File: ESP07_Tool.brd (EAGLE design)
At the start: 34 x 36.3 mm, 38 parts

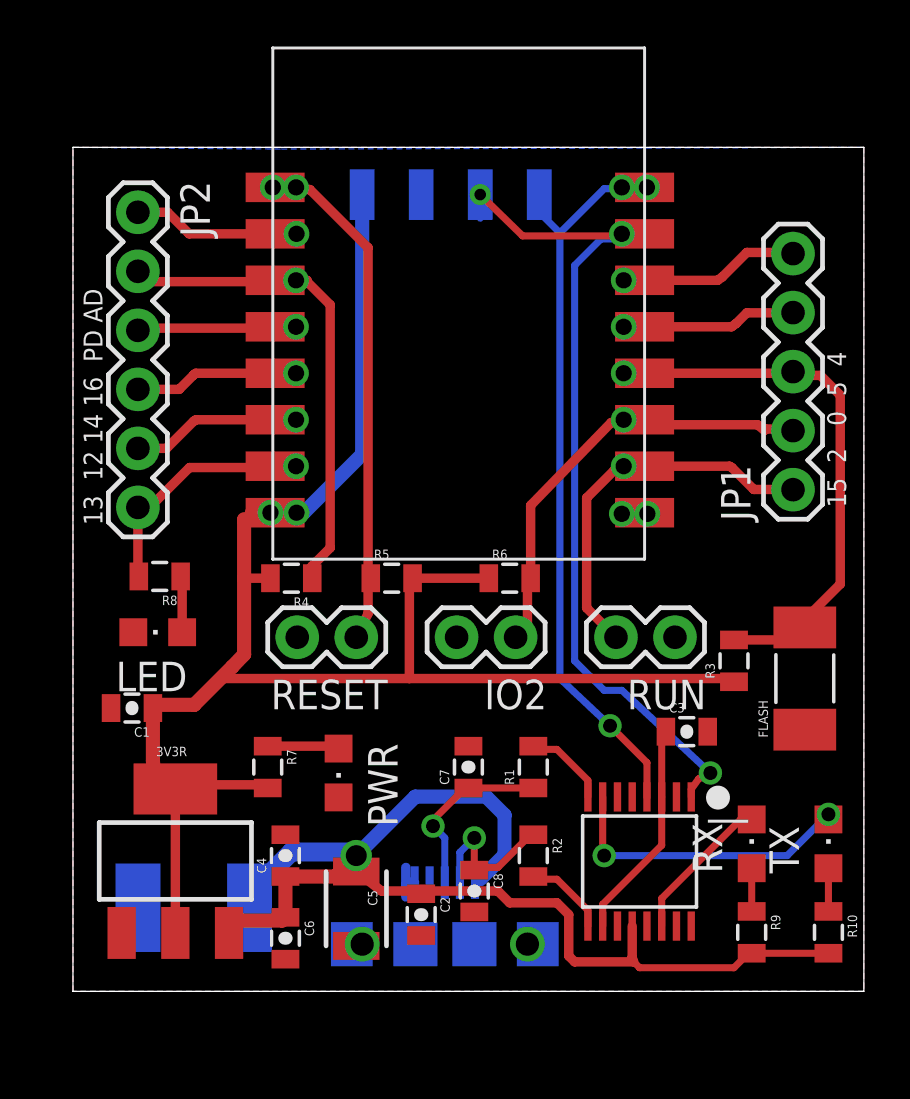
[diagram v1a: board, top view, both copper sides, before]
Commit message: Mods after actual use
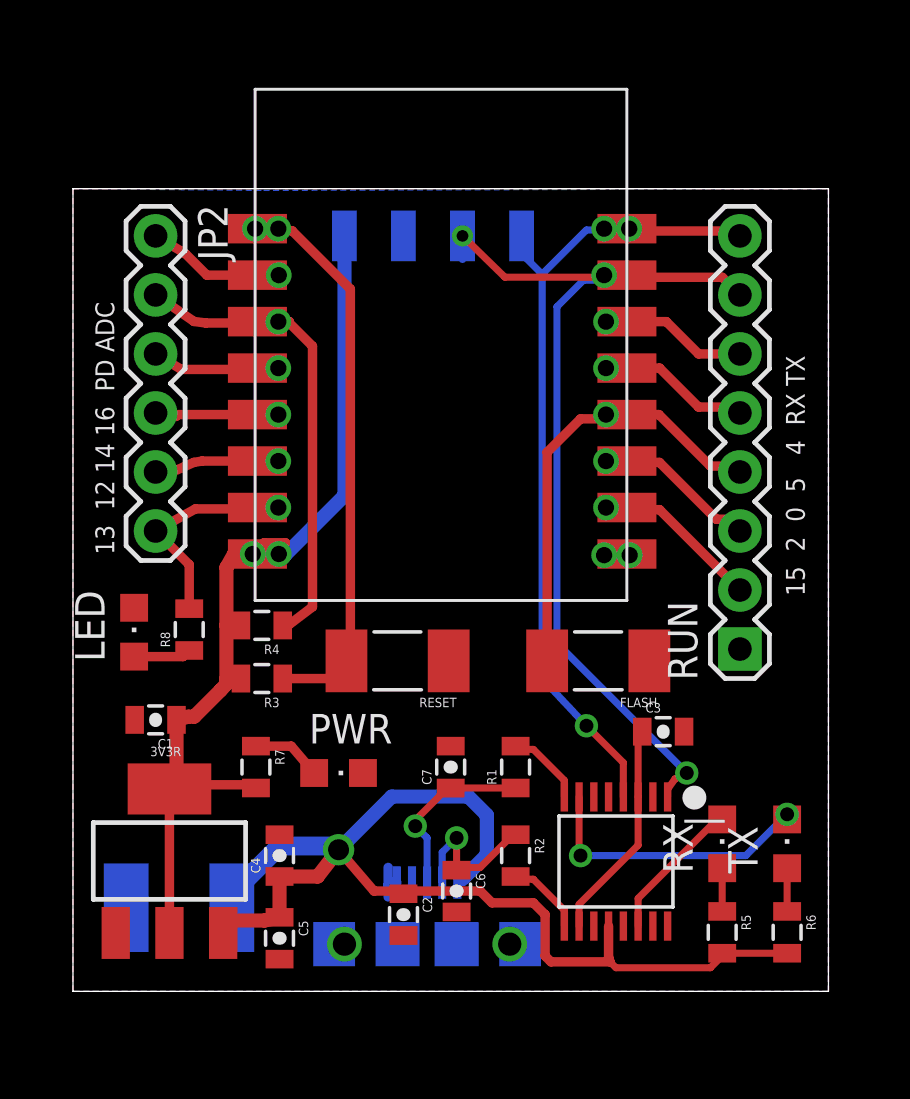
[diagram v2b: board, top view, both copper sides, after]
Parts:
- removed C8: 47pF, SparkFun-Capacitors:0805-CAP
- removed IO2: (no value), SparkFun-Connectors:1X02
- removed JP1: (no value), SparkFun-Connectors:1X05
- removed R10, R9: 330, SparkFun-Resistors:0805
- C1, C2: value 10uF -> 1uF
- C5: value 4.7uF -> 0.1uF; device SparkFun-Capacitors:1210 -> SparkFun-Capacitors:0805-CAP
- C6: value 0.1uF -> 47pF
- R5, R6: value 10K -> 330
- RESET: device SparkFun-Connectors:1X02 -> SparkFun-Resistors:R2010
- RUN: device SparkFun-Connectors:1X02 -> SparkFun-Connectors:1X08
- moved R5 20.8 mm to (27.9, 2.54), turned to 270 degrees
- moved R3 20.3 mm to (8.13, 13.5), turned to 180 degrees
- moved R6 19.4 mm to (30.7, 2.54), turned to 270 degrees
- moved FLASH 8.92 mm to (22.6, 14.2), turned to 180 degrees
- moved C6 7.64 mm to (16.5, 4.32)
- moved C5 3.54 mm to (8.89, 2.29)
- moved RUN 2.84 mm to (28.7, 14.7), turned to 90 degrees
- moved R8 2.62 mm to (5.00, 15.6), turned to 90 degrees
- moved R4 2.40 mm to (8.13, 15.7)
- moved RESET 2.05 mm to (14.0, 14.2)
- moved U$1 1.93 mm to (7.84, 16.8)
- moved U$4 1.93 mm to (16.8, 32.5)
- moved U$5 1.93 mm to (19.3, 32.5)
- moved U$6 1.93 mm to (11.7, 32.5)
- moved U$7 1.93 mm to (14.2, 32.5)
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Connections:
- net 3V3: now also R3.2; no longer R3.1, R5.2, R6.1
- net GND: now also RESET.1; no longer C8.2, IO2.2, RESET.2
- net N$10: now also RUN.4; no longer JP1.3, R3.2
- net N$14: now also R5.1; no longer R9.1
- net N$19: now also R6.1; no longer R10.1
- net N$22: now also R3.1, RESET.2; no longer R5.1, RESET.1
- net N$23: now also C6.1; no longer C8.1
- net N$3: now also RUN.6; no longer JP1.5
- net N$7: now also RUN.3; no longer IO2.1, JP1.2, R6.2
- net N$8: no longer JP1.1
- net N$9: now also RUN.5; no longer JP1.4
- net RXD: now also RUN.7
- net TXD: now also RUN.8
- net VCC: now also R5.2, R6.2; no longer C6.1, R10.2, R9.2
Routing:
- net 3V3: track 78.3 -> 46.2 mm
- net N$7: track 20.0 -> 7.86 mm
- net N$8: track 17.7 -> 7.64 mm
- net N$10: track 24.4 -> 19.0 mm
- net TXD: track 33.9 -> 36.2 mm
- net N$22: track 24.6 -> 26.6 mm
- net N$17: track 7.31 -> 5.37 mm
- net RXD: track 40.6 -> 42.4 mm
- net N$16: track 7.12 -> 5.36 mm
- net N$3: track 7.79 -> 6.34 mm
- net N$15: track 6.90 -> 5.53 mm
- net N$12: track 11.4 -> 10.1 mm
- net N$11: track 21.5 -> 20.4 mm
- net N$18: track 10.6 -> 9.53 mm
- net VCC: track 51.7 -> 50.7 mm
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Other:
- board size 34 x 36.3 mm -> 32.5 x 34.5 mm
- board text added: "13 12 14 16 PD ADC"
- board text added: "15 2 0 5 4 RX TX"
- board text removed: "13 12 14 16 PD AD"
- board text removed: "15 2 0 5 4"

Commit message: Added 3v3 and gnd header pins
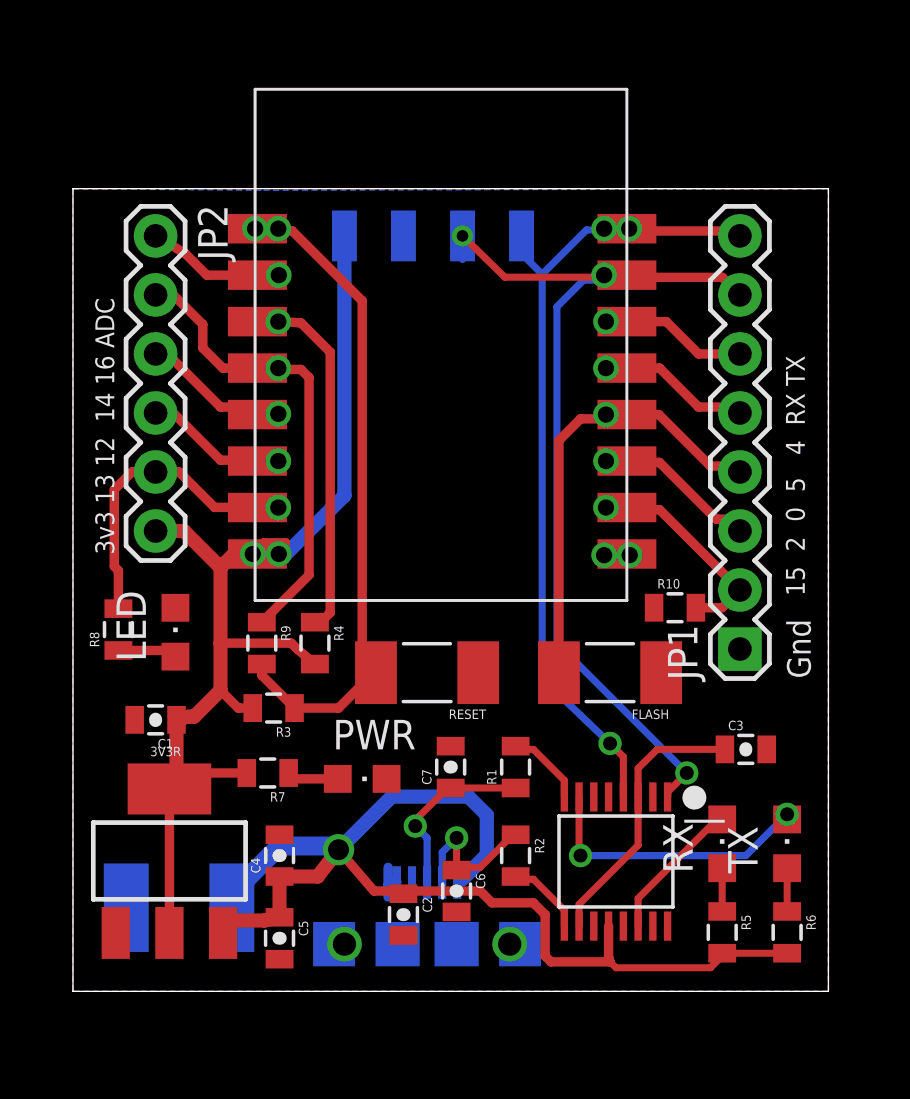
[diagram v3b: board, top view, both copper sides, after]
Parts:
- added R10, R9: 10K, SparkFun-Resistors:0805
- moved C3 3.64 mm to (29.0, 10.4)
- moved R8 3.05 mm to (1.96, 15.6)
- moved R4 2.41 mm to (10.4, 15.0), turned to 270 degrees
- moved LED 1.78 mm to (4.41, 15.5)
- moved RESET 1.37 mm to (15.2, 13.7)
- moved R3 1.37 mm to (8.64, 12.2)
- moved PWR 1.05 mm to (12.4, 9.14)
- moved FLASH 0.72 mm to (23.1, 13.7)
- moved R7 0.57 mm to (8.38, 9.40), turned to 180 degrees
- renumbered RUN to JP1
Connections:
- removed net N$16: JP2.4, U$1.GPIO14
- new net N$1: JP2.3, U$1.GPIO14
- net 3V3: now also JP2.6
- net GND: now also R10.1
- net N$11: no longer JP2.2
- net N$15: now also JP2.2, R9.1; no longer JP2.3
- net N$17: now also JP2.4; no longer JP2.5
- net N$18: now also JP2.5; no longer JP2.6
- net N$22: now also R9.2
- net N$8: now also R10.2
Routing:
- net N$15: track 5.53 -> 21.0 mm
- net 3V3: track 46.2 -> 54.7 mm
- net N$1: track 0.00 -> 6.31 mm, vias 0 -> 1
- net N$16: track 5.36 -> 0.00 mm, vias 1 -> 0
- net N$11: track 20.4 -> 15.9 mm
- net N$22: track 26.6 -> 31.0 mm
- net N$18: track 9.53 -> 13.3 mm
- net N$5: track 9.47 -> 11.9 mm
- net N$8: track 7.64 -> 9.85 mm
- net N$4: track 3.04 -> 2.22 mm
- net N$17: track 5.37 -> 6.14 mm
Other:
- board text added: "3v3 13 12 14 16 ADC"
- board text added: "Gnd"
- board text removed: "13 12 14 16 PD ADC"

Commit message: Switched to MCP1824ST-3302E/DB
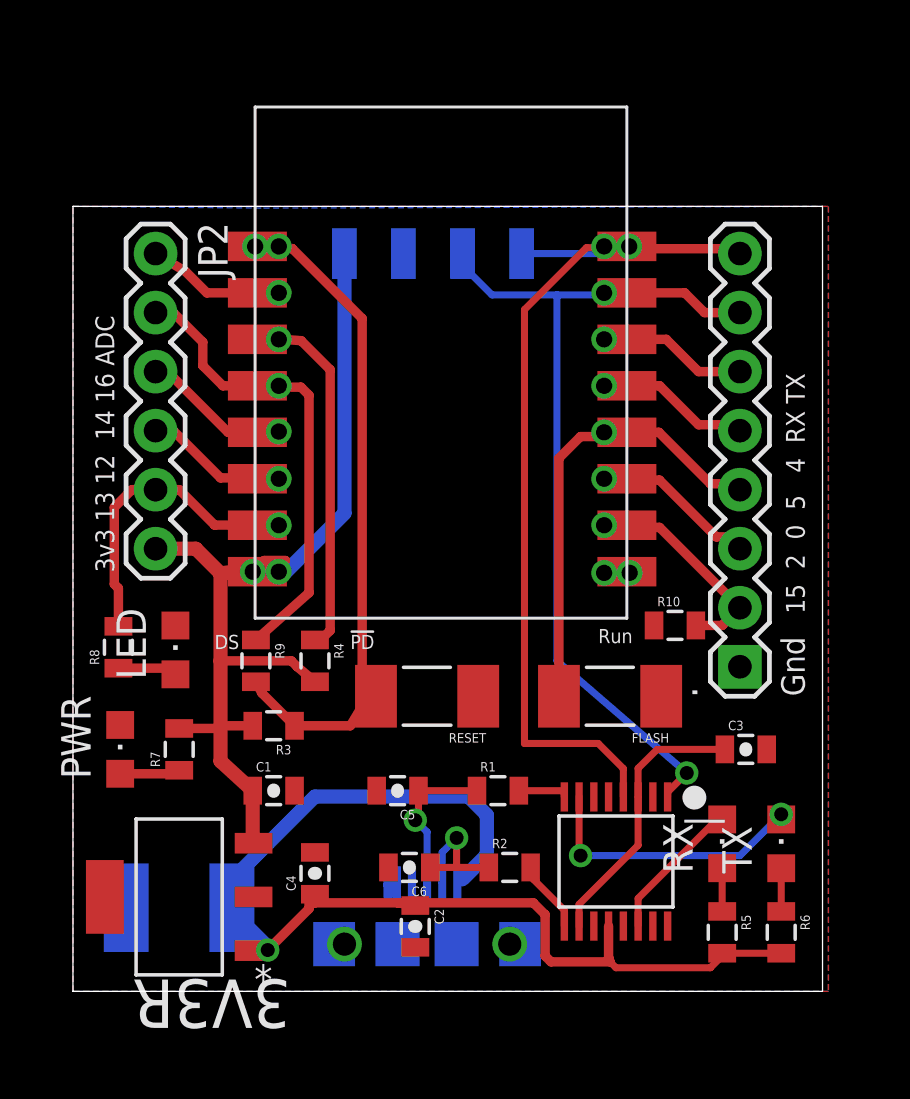
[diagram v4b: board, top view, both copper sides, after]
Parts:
- removed C7: 47pF, SparkFun-Capacitors:0805-CAP
- removed JP1: (no value), SparkFun-Connectors:1X08
- added .: (no value), SparkFun-Connectors:1X08
- 3V3R: value (none) -> MCP1824ST-3302E/DB; device SparkFun-PowerIC:SOT223 -> Microchip_By_element14_Batch_1:SOT230P700X180-4N
- C4: value 0.01uF -> 0.1uF
- C5: value 0.1uF -> 47pF
- moved PWR 10.5 mm to (2.03, 10.4), turned to 0 degrees
- moved C5 8.13 mm to (14.0, 8.64), turned to 180 degrees
- moved C1 5.92 mm to (8.64, 8.64), turned to 0 degrees
- moved R7 3.94 mm to (4.57, 10.4), turned to 90 degrees
- moved C6 2.27 mm to (14.5, 5.33), turned to 180 degrees
- moved C4 1.70 mm to (10.4, 5.08)
- moved 3V3R 1.60 mm to (4.57, 4.06), turned to 180 degrees
- moved R1 1.27 mm to (18.3, 8.64), turned to 0 degrees
- moved FLASH 1.02 mm to (23.1, 12.7)
- moved RESET 1.02 mm to (15.2, 12.7)
- moved R9 0.80 mm to (7.87, 14.2)
- moved R10 0.76 mm to (25.9, 15.7)
- moved JP2 0.76 mm to (3.56, 31.8)
- moved R3 0.76 mm to (8.64, 11.4)
- moved R4 0.76 mm to (10.4, 14.2)
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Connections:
- net 3V3: now also 3V3R.3; no longer 3V3R.2, 3V3R.4
- net GND: now also ..1, 3V3R.2, 3V3R.4; no longer 3V3R.1, C7.2, JP1.1
- net N$10: now also ..4; no longer JP1.4
- net N$26: now also C5.1; no longer C7.1
- net N$3: now also ..6; no longer JP1.6
- net N$7: now also ..3; no longer JP1.3
- net N$8: now also ..2; no longer JP1.2
- net N$9: now also ..5; no longer JP1.5
- net RXD: now also ..7; no longer JP1.7
- net TXD: now also ..8; no longer JP1.8
- net VCC: now also 3V3R.1; no longer 3V3R.3, C5.1
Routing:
- net 3V3: track 54.7 -> 46.5 mm
- net RXD: track 42.3 -> 38.7 mm, vias 3 -> 2
- net TXD: track 36.3 -> 39.8 mm, vias 3 -> 2
- net N$12: track 10.1 -> 7.88 mm
- net N$16: track 0.00 -> 2.05 mm
- net N$21: track 3.42 -> 2.21 mm
- net N$26: track 7.79 -> 6.74 mm
- net VCC: track 50.7 -> 49.8 mm
- net N$23: track 6.70 -> 6.11 mm
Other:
- board size 32.5 x 34.5 mm -> 32.3 x 33.8 mm
- board text added: "!PD"
- board text added: "6Vmax"
- board text added: "DS"
- board text added: "Run"
- board text removed: "15Vmax"
